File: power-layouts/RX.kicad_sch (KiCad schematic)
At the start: 43 parts, among them J401 RX_IN, J402 PREAMP, J403 BIAS_RES, J404 BIAS_RES, J405 GAIN_RES, J406 LPF_CAP, J407 VARAMP_OUT, U401 MD0100DK6-G, U402 OPA1612AIDR, U403 AD8338ACPZ-R7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

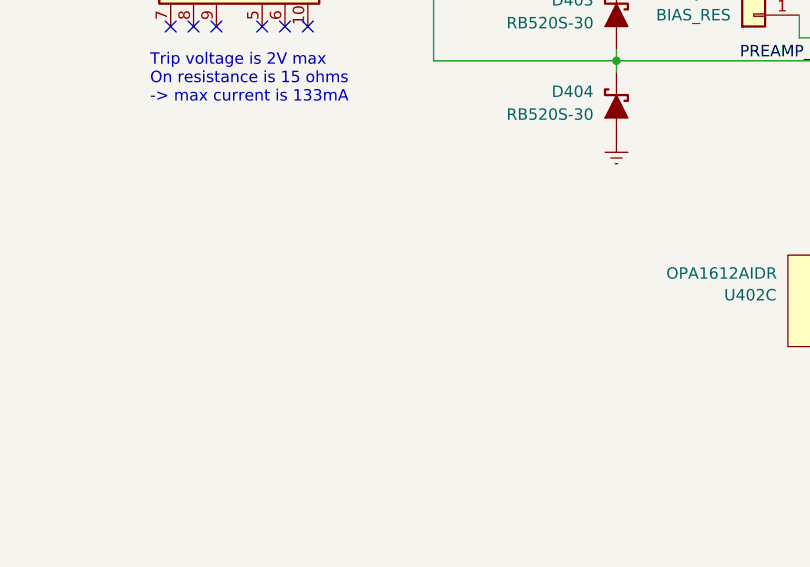
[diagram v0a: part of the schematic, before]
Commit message: added RF Shield
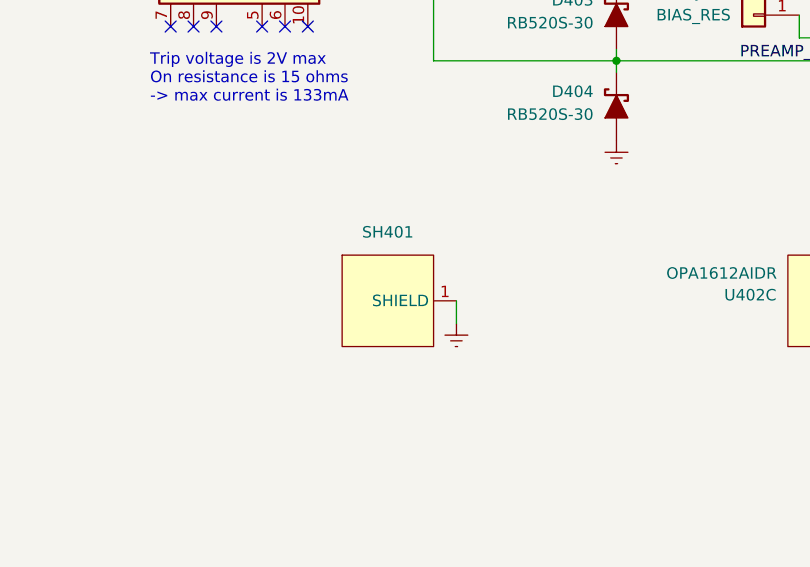
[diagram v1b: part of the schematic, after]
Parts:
- added SH401: 44-CBSA-1.0X1.5X0.4, BR_Electromechanical:44-CBSA-1.0X1.5X0.4, symbol BR_Electromechanical:44-CBSA-1.0X1.5X0.4
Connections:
- net GND: now also SH401.1 (SHIELD)
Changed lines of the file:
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@@
 	(wire
 		(pts
+			(xy 101.6 182.88) (xy 101.6 185.42)
+		)
+		(stroke
+			(width 0)
+			(type default)
+		)
+	)
+	(wire
+		(pts
 			(xy 335.28 139.7) (xy 335.28 129.54)
 		)
@@
 	(symbol
 		(lib_id "BR_Virtual_Parts:GND")
+		(at 101.6 185.42 0)
+		(unit 1)
+		(exclude_from_sim no)
+		(in_bom yes)
+		(on_board yes)
+		(dnp no)
+		(fields_autoplaced yes)
+		(property "Reference" "#PWR0415"
+			(at 101.6 191.77 0)
+			(effects
+				(font
+					(size 1.27 1.27)
+				)
+				(hide yes)
+			)
+		)
+		(property "Value" "GND"
+			(at 101.6 190.5 0)
+			(effects
+				(font
+					(size 1.27 1.27)
+				)
+				(hide yes)
+			)
+		)
+		(property "Footprint" ""
+			(at 101.6 185.42 0)
+			(effects
+				(font
+					(size 1.27 1.27)
+				)
+				(hide yes)
+			)
+		)
+		(property "Datasheet" ""
+			(at 101.6 185.42 0)
+			(effects
+				(font
+					(size 1.27 1.27)
+				)
+				(hide yes)
+			)
+		)
+		(property "Description" ""
+			(at 101.6 185.42 0)
+			(effects
+				(font
+					(size 1.27 1.27)
+				)
+				(hide yes)
+			)
+		)
+		(pin "1"
+		)
+		(instances
+			(project "sonar-dev-board-power-layouts"
+				(path "/2a5ce3ef-537a-4122-a1be-ef76186bc0d7/75372584-e821-4a7e-ae66-bcf96239ddf7"
+					(reference "#PWR0415")
+					(unit 1)
+				)
+			)
+		)
+	)
+	(symbol
+		(lib_id "BR_Virtual_Parts:GND")
 		(at 283.21 101.6 0)
 		(mirror y)
@@
 					(unit 1)
 				)
+			)
+		)
+	)
+	(symbol
+		(lib_id "BR_Electromechanical:44-CBSA-1.0X1.5X0.4")
+		(at 88.9 177.8 0)
+		(unit 1)
+		(exclude_from_sim no)
+		(in_bom yes)
+		(on_board yes)
+		(dnp no)
+		(fields_autoplaced yes)
+		(property "Reference" "SH401"
+			(at 93.98 175.26 0)
+			(effects
+				(font
+					(size 1.27 1.27)
+				)
+			)
+		)
+		(property "Value" "44-CBSA-1.0X1.5X0.4"
+			(at 88.9 177.8 0)
+			(effects
+				(font
+					(size 1.27 1.27)
+				)
+				(hide yes)
+			)
+		)
+		(property "Footprint" "BR_Electromechanical:44-CBSA-1.0X1.5X0.4"
+			(at 88.9 101.6 0)
+			(effects
+				(font
+					(size 1.27 1.27)
+				)
+				(justify left)
+				(hide yes)
+			)
+		)
+		(property "Datasheet" "https://www.leadertechinc.com/assets/files/catalogs/cbs.pdf"
+			(at 88.9 104.14 0)
+			(effects
+				(font
+					(size 1.27 1.27)
+				)
+				(justify left)
+				(hide yes)
+			)
+		)
+		(property "Description" "RF Shield Shield, 2-Piece 1.000\" (25.40mm) X 1.500\" (38.10mm) Non-Vented Through Hole"
+			(at 88.9 106.68 0)
+			(effects
+				(font
+					(size 1.27 1.27)
+				)
+				(justify left)
+				(hide yes)
+			)
+		)
+		(property "Manufacturer" "Leader Tech Inc."
+			(at 88.9 109.22 0)
+			(effects
+				(font
+					(size 1.27 1.27)
+				)
+				(justify left)
+				(hide yes)
+			)
+		)
+		(property "Manufacturer Part Num" "44-CBSA-1.0X1.5X0.4"
+			(at 88.9 111.76 0)
+			(effects
+				(font
+					(size 1.27 1.27)
+				)
+				(justify left)
+				(hide yes)
+			)
+		)
+		(property "BRE Number" "BRE-001302"
+			(at 88.9 114.3 0)
+			(effects
+				(font
+					(size 1.27 1.27)
+				)
+				(justify left)
+				(hide yes)
+			)
+		)
+		(property "JLCPCB Part Num" ""
+			(at 88.9 116.84 0)
+			(effects
+				(font
+					(size 1.27 1.27)
+				)
+				(justify left)
+				(hide yes)
+			)
+		)
+		(pin "1"
+		)
+		(instances
+			(project "sonar-dev-board-power-layouts"
+				(path "/2a5ce3ef-537a-4122-a1be-ef76186bc0d7/75372584-e821-4a7e-ae66-bcf96239ddf7"
+					(reference "SH401")
+					(unit 1)
+				)
